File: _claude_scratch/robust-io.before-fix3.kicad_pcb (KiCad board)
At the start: 4 copper layers, 160 x 100 mm, 304 parts, among them J1 AVR-ISP-6, J10 Screw_Terminal_01x06, J14 Screw_Terminal_01x04, J15 Screw_Terminal_01x04, J16 Screw_Terminal_01x06, J18 Screw_Terminal_01x06, J19 Screw_Terminal_01x06, J20 UART, J3 Screw_Terminal_01x06, J4 Screw_Terminal_01x04, J5 Screw_Terminal_01x06, J6 Screw_Terminal_01x06, J9 Screw_Terminal_01x06, Q3 2N7002, Q4 2N7002, SW1 CHS-01TB, SW2 B3U-1000P, U1 DRV8876, U10 BTS7008, U11 BTS7008, U14 DRV8876, U2 ATmega1284P-A, U3 MCP2515, U4 TPS5604, U5 TPS5604, U6 MCP2562-E-MF, U7 MC33978, U8 BTS7008, U9 BTS7008, Y1 16MHz, Y2 12MHz

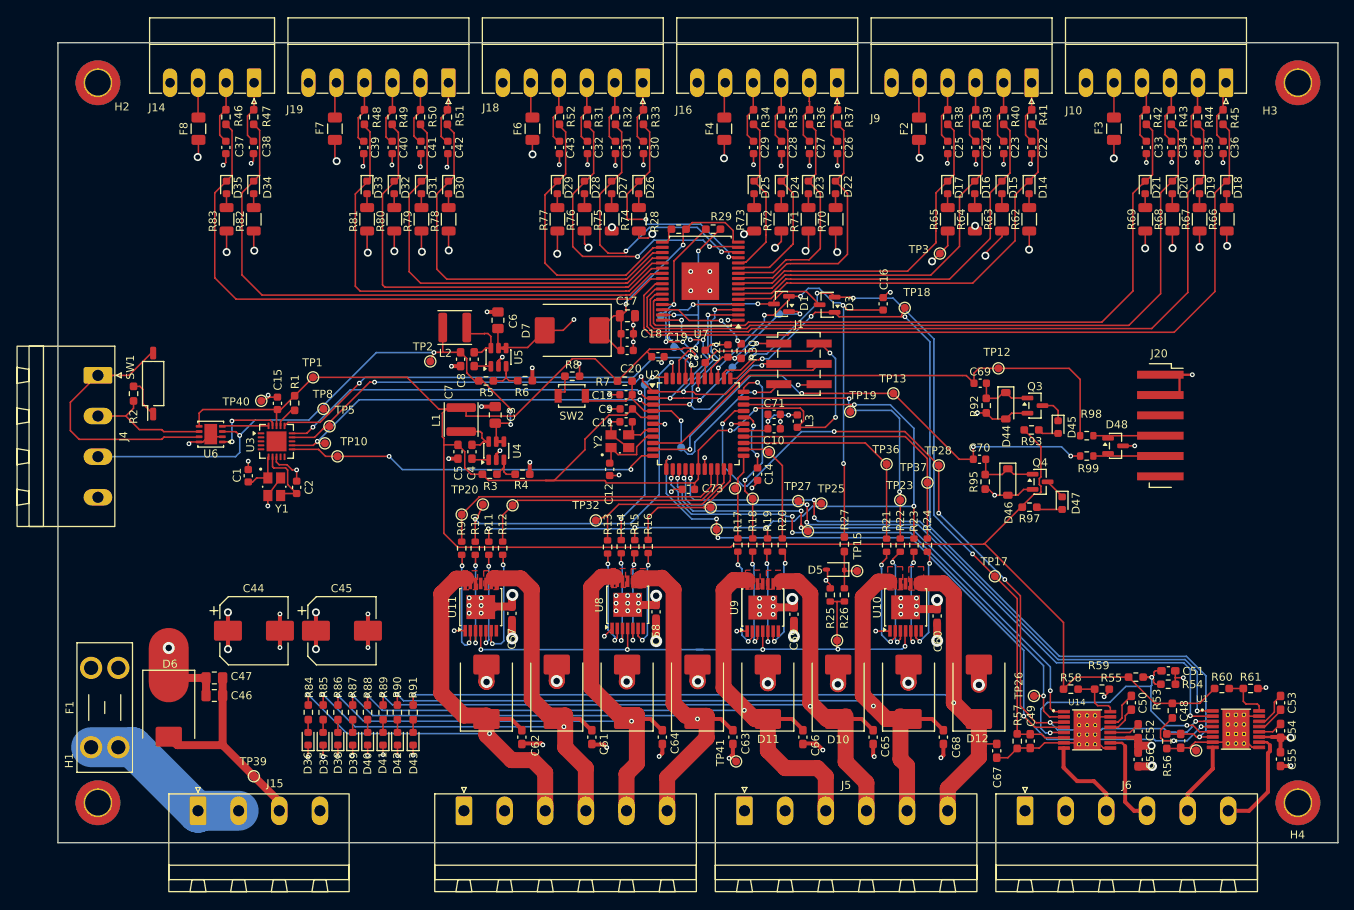
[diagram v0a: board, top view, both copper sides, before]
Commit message: Rev A: release to fab (JLCPCB, 5 PCB / 2 assembled)
Board
- Outline set to exactly 160 x 100 mm; plane zones resized to match
- UART brought out on J20 (1x6 SMD, FTDI pinout) with series
  resistors R98/R99 and TVS D48
- J1 and J20 changed to SMD headers (C52016780, C41417363)
- L1/L2 moved to Sunlord SWPA4030S footprints; regulator tracks rerouted
- 41 test points added (35 top, 6 bottom), including SPI access
- Crystal case pins (Y1/Y2 pads 2, 4) tied to GND
- SW2 changed to 2-pin push button symbol
- R84-R91 changed from 2.2k to 10k to cut dissipation at 24 V
- Thermal vias in U1/U14 enlarged to 0.3 mm drill; 27 +24V vias added
  under U8-U11; solid plane connections on high-current pins
- Input/output rows and edge connectors aligned
- /inputs/_SG4 track and via moved clear of R74 pad 1

Schematic
- ERC cleared: no-connects, PWR_FLAGs, pin types, off-grid items
- Symbols moved to project library robust-io
- Test point symbols added on processor and power sheets

Rules
- Custom DRC rule for U7 pad-to-pad clearance (0.15 mm)
- Minimum through hole 0.2 mm; silk-to-edge check ignored

Fab outputs (fab/)
- make_gerbers.sh: Gerbers, drill and position export via kicad-cli
- JLC BOM with LCSC part numbers on all 50 SMD lines
- JLC placement file with per-part rotation offsets
  (cpl_rotation_offsets.json), verified in JLC placement preview
- Through-hole BOM and test point list

DRC: 4 library-mismatch warnings (J20, U1, U14, U7), 0 errors
ERC: clean
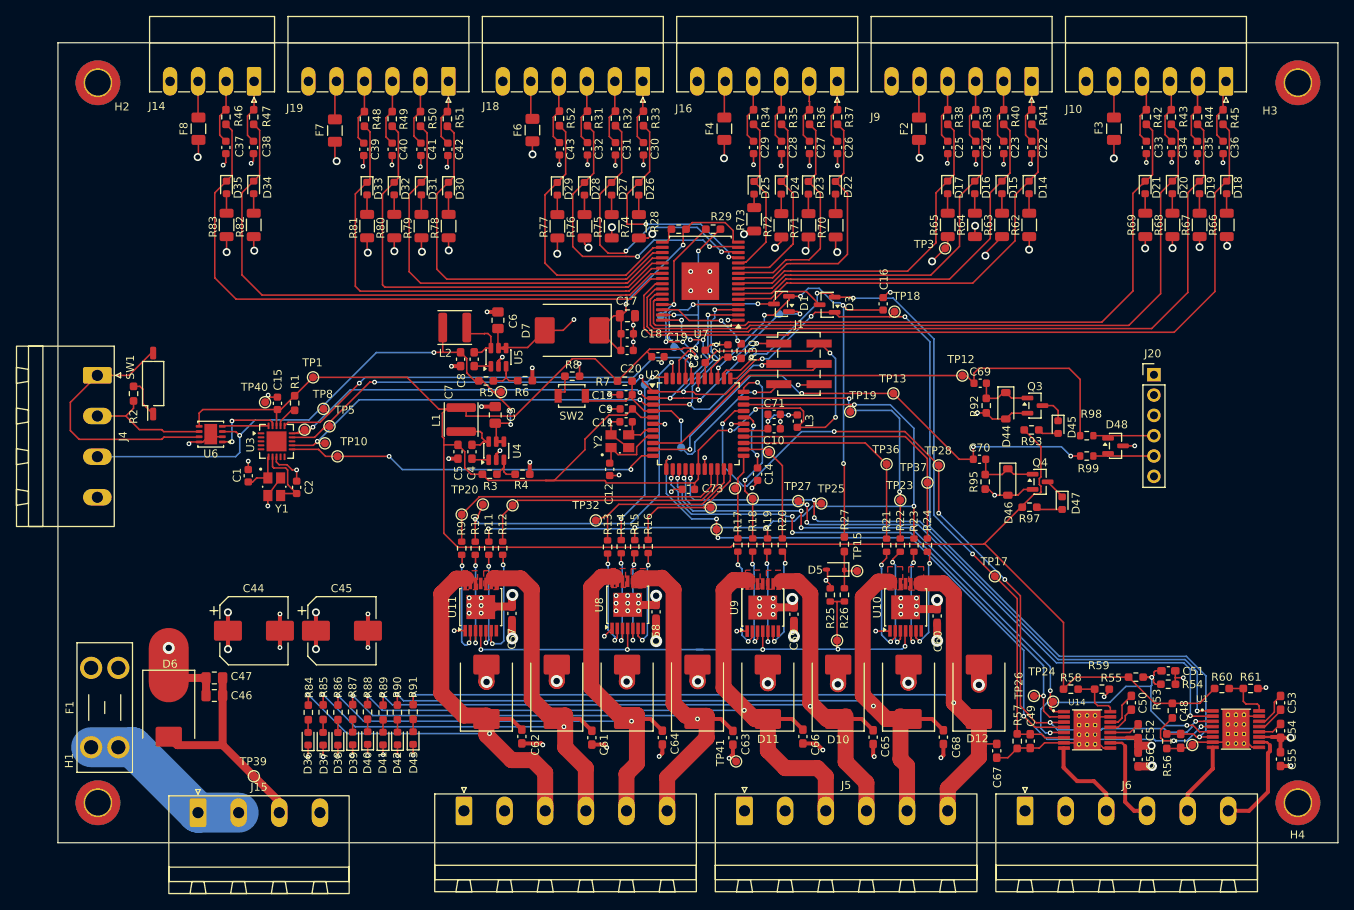
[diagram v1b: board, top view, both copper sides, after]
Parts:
- J20: footprint Connector_PinHeader_2.54mm:PinHeader_1x06_P2.54mm_Vertical_SMD_Pin1Right -> Connector_PinHeader_2.54mm:PinHeader_1x06_P2.54mm_Vertical
- TP6: moved to F.Cu
- moved TP6 54.0 mm to (60.8, 78.4)
- moved TP24 37.3 mm to (154.4, 112.4)
- moved TP2 9.63 mm to (85.4, 73.7)
- moved J20 6.40 mm to (167.0, 71.5)
- moved TP12 4.60 mm to (143.1, 71.6)
- moved TP18 1.36 mm to (134.6, 63.6)
- moved TP3 0.92 mm to (140.9, 55.7)
- moved R74 0.87 mm to (102.6, 52.9)
- moved R75 0.87 mm to (99.2, 52.9)
- moved R76 0.87 mm to (95.8, 52.9)
- moved R77 0.87 mm to (92.4, 52.9)
- moved R78 0.85 mm to (78.8, 52.9)
- moved R79 0.85 mm to (75.4, 52.9)
- moved R80 0.85 mm to (72.0, 52.9)
- moved R81 0.85 mm to (68.6, 52.9)
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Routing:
- net +24V: track 131.6 -> 118.2 mm
- net GND: track 258.0 -> 251.2 mm, vias 103 -> 102
- net MISO0: track 83.1 -> 84.3 mm
- net Net-(D29-A): track 1.74 -> 2.44 mm
- net Net-(D33-A): track 1.74 -> 2.44 mm
- net Net-(D32-A): track 1.74 -> 2.44 mm
- net Net-(D30-A): track 1.74 -> 2.44 mm
- net Net-(D28-A): track 1.74 -> 2.44 mm
- net Net-(D26-A): track 1.74 -> 2.44 mm
- net Net-(D23-A): track 1.74 -> 2.44 mm
- net Net-(D35-A): track 1.74 -> 2.44 mm
- net Net-(D34-A): track 1.74 -> 2.44 mm
- net Net-(D24-A): track 1.74 -> 2.44 mm
- net Net-(D22-A): track 1.74 -> 2.44 mm
- net Net-(D21-A): track 1.74 -> 2.44 mm
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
